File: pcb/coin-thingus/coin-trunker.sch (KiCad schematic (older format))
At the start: 30 parts, among them J1 6P6C, J2 6P6C, J3 Conn_02x20_Odd_Even, J4 Barrel_Jack_Switch_MountingPin, J5 Screw_Terminal_01x02, K1 AGQ200A4, K2 AGQ200A4, Q1 BSS123L, U1 ULN2003LV, U4 TCA9534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

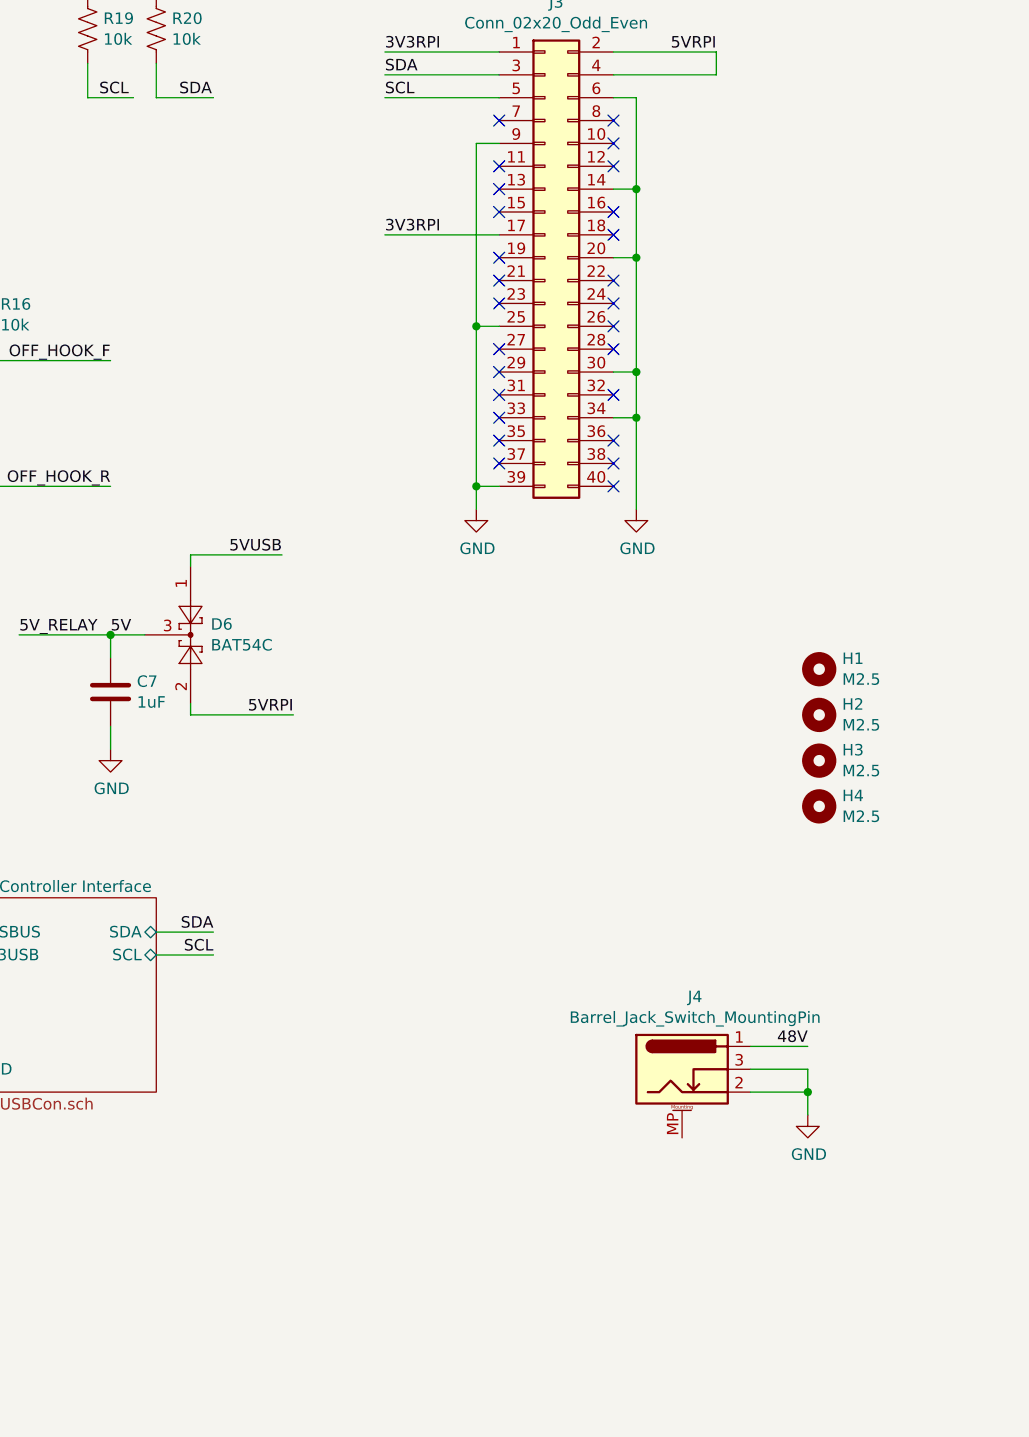
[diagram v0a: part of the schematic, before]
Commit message: Add CERN-OHL-W v2 license
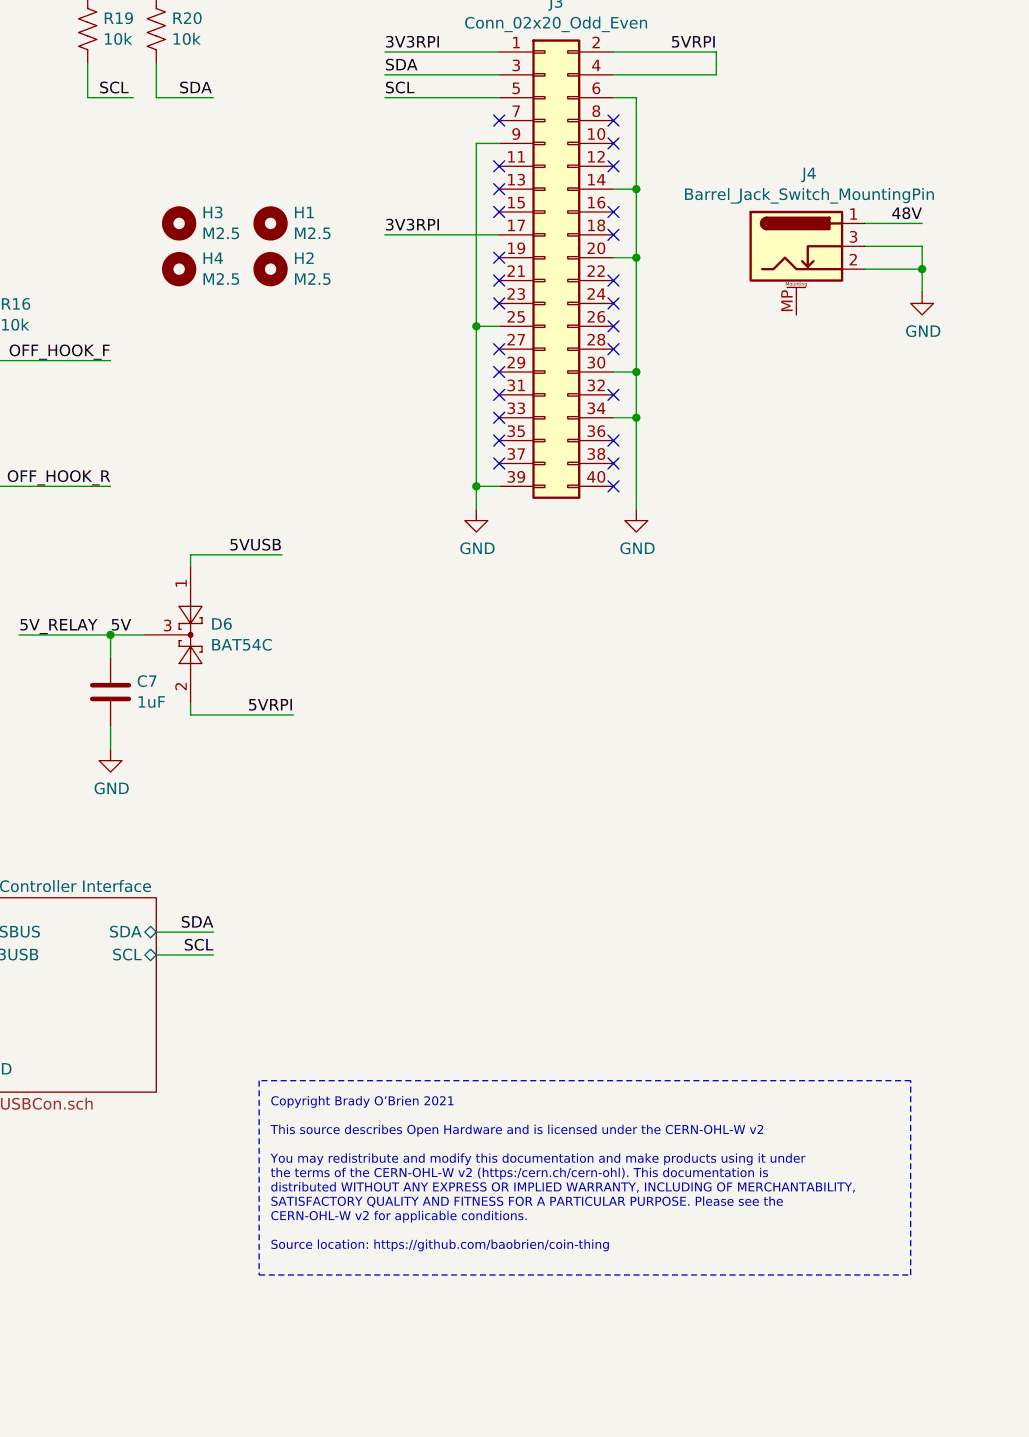
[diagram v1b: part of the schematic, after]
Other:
- note added: "Copyright Brady O’Brien 2021\n\nThis source describes Open Hardware and is licensed under the CERN-OHL-W v2\n\nYou may redistribute and modify this documentation and make products using it under\nthe terms of the CERN-OHL-W v2 (https:/cern.ch/cern-ohl). This documentation is\ndistributed WITHOUT ANY EXPRESS OR IMPLIED WARRANTY, INCLUDING OF MERCHANTABILITY,\nSATISFACTORY QUALITY AND FITNESS FOR A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"
- moved on the sheet: H1, H2, H3, H4, J4
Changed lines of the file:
@@
 L Connector:Barrel_Jack_Switch_MountingPin J4
 U 1 1 5F9413CC
-P 9850 5400
-F 0 "J4" H 9907 5717 50  0000 C CNN
-F 1 "Barrel_Jack_Switch_MountingPin" H 9907 5626 50  0000 C CNN
-F 2 "Connector_BarrelJack:BarrelJack_CUI_PJ-102AH_Horizontal" H 9900 5360 50  0001 C CNN
-F 3 "~" H 9900 5360 50  0001 C CNN
-F 4 "PJ-102AH" H 9850 5400 50  0001 C CNN "Part"
-	1    9850 5400
+P 10350 1800
+F 0 "J4" H 10407 2117 50  0000 C CNN
+F 1 "Barrel_Jack_Switch_MountingPin" H 10407 2026 50  0000 C CNN
+F 2 "Connector_BarrelJack:BarrelJack_CUI_PJ-102AH_Horizontal" H 10400 1760 50  0001 C CNN
+F 3 "~" H 10400 1760 50  0001 C CNN
+F 4 "PJ-102AH" H 10350 1800 50  0001 C CNN "Part"
+	1    10350 1800
 	1    0    0    -1
 $EndComp
@@
 L power:GND #PWR0101
 U 1 1 5F942022
-P 10400 5600
-F 0 "#PWR0101" H 10400 5350 50  0001 C CNN
-F 1 "GND" H 10405 5427 50  0000 C CNN
-F 2 "" H 10400 5600 50  0001 C CNN
-F 3 "" H 10400 5600 50  0001 C CNN
-	1    10400 5600
-	1    0    0    -1
-$EndComp
-Wire Wire Line
-	10150 5400 10400 5400
-Wire Wire Line
-	10400 5400 10400 5500
-Wire Wire Line
-	10150 5500 10400 5500
-Connection ~ 10400 5500
-Wire Wire Line
-	10400 5500 10400 5600
-Wire Wire Line
-	10400 5300 10150 5300
-Text Label 10400 5300 2    50   ~ 0
+P 10900 2000
+F 0 "#PWR0101" H 10900 1750 50  0001 C CNN
+F 1 "GND" H 10905 1827 50  0000 C CNN
+F 2 "" H 10900 2000 50  0001 C CNN
+F 3 "" H 10900 2000 50  0001 C CNN
+	1    10900 2000
+	1    0    0    -1
+$EndComp
+Wire Wire Line
+	10650 1800 10900 1800
+Wire Wire Line
+	10900 1800 10900 1900
+Wire Wire Line
+	10650 1900 10900 1900
+Connection ~ 10900 1900
+Wire Wire Line
+	10900 1900 10900 2000
+Wire Wire Line
+	10900 1700 10650 1700
+Text Label 10900 1700 2    50   ~ 0
 48V
 $Sheet
@@
 L Mechanical:MountingHole H1
 U 1 1 5FDD0277
-P 10450 3650
-F 0 "H1" H 10550 3696 50  0000 L CNN
-F 1 "M2.5" H 10550 3605 50  0000 L CNN
-F 2 "MountingHole:MountingHole_2.7mm_M2.5_Pad" H 10450 3650 50  0001 C CNN
-F 3 "~" H 10450 3650 50  0001 C CNN
-	1    10450 3650
+P 8050 1700
+F 0 "H1" H 8150 1746 50  0000 L CNN
+F 1 "M2.5" H 8150 1655 50  0000 L CNN
+F 2 "MountingHole:MountingHole_2.7mm_M2.5_Pad" H 8050 1700 50  0001 C CNN
+F 3 "~" H 8050 1700 50  0001 C CNN
+	1    8050 1700
 	1    0    0    -1
 $EndComp
@@
 L Mechanical:MountingHole H2
 U 1 1 5FDDD6B4
-P 10450 3850
-F 0 "H2" H 10550 3896 50  0000 L CNN
-F 1 "M2.5" H 10550 3805 50  0000 L CNN
-F 2 "MountingHole:MountingHole_2.7mm_M2.5_Pad" H 10450 3850 50  0001 C CNN
-F 3 "~" H 10450 3850 50  0001 C CNN
-	1    10450 3850
+P 8050 1900
+F 0 "H2" H 8150 1946 50  0000 L CNN
+F 1 "M2.5" H 8150 1855 50  0000 L CNN
+F 2 "MountingHole:MountingHole_2.7mm_M2.5_Pad" H 8050 1900 50  0001 C CNN
+F 3 "~" H 8050 1900 50  0001 C CNN
+	1    8050 1900
 	1    0    0    -1
 $EndComp
@@
 L Mechanical:MountingHole H3
 U 1 1 5FDDDD20
-P 10450 4050
-F 0 "H3" H 10550 4096 50  0000 L CNN
-F 1 "M2.5" H 10550 4005 50  0000 L CNN
-F 2 "MountingHole:MountingHole_2.7mm_M2.5_Pad" H 10450 4050 50  0001 C CNN
-F 3 "~" H 10450 4050 50  0001 C CNN
-	1    10450 4050
+P 7650 1700
+F 0 "H3" H 7750 1746 50  0000 L CNN
+F 1 "M2.5" H 7750 1655 50  0000 L CNN
+F 2 "MountingHole:MountingHole_2.7mm_M2.5_Pad" H 7650 1700 50  0001 C CNN
+F 3 "~" H 7650 1700 50  0001 C CNN
+	1    7650 1700
 	1    0    0    -1
 $EndComp
@@
 L Mechanical:MountingHole H4
 U 1 1 5FDDDF7B
-P 10450 4250
-F 0 "H4" H 10550 4296 50  0000 L CNN
-F 1 "M2.5" H 10550 4205 50  0000 L CNN
-F 2 "MountingHole:MountingHole_2.7mm_M2.5_Pad" H 10450 4250 50  0001 C CNN
-F 3 "~" H 10450 4250 50  0001 C CNN
-	1    10450 4250
+P 7650 1900
+F 0 "H4" H 7750 1946 50  0000 L CNN
+F 1 "M2.5" H 7750 1855 50  0000 L CNN
+F 2 "MountingHole:MountingHole_2.7mm_M2.5_Pad" H 7650 1900 50  0001 C CNN
+F 3 "~" H 7650 1900 50  0001 C CNN
+	1    7650 1900
 	1    0    0    -1
 $EndComp
@@
 Wire Wire Line
 	3000 3650 3650 3650
+Text Notes 8050 6200 0    39   ~ 0
+Copyright Brady O’Brien 2021\n\nThis source describes Open Hardware and is licensed under the CERN-OHL-W v2\n\nYou may redistribute and modify this documentation and make products using it under\nthe terms of the CERN-OHL-W v2 (https:/cern.ch/cern-ohl). This documentation is\ndistributed WITHOUT ANY EXPRESS OR IMPLIED WARRANTY, INCLUDING OF MERCHANTABILITY,\nSATISFACTORY QUALITY AND FITNESS FOR A PARTICULAR PURPOSE. Please see the\nCERN-OHL-W v2 for applicable conditions.\n\nSource location: https://github.com/baobrien/coin-thing
+Wire Notes Line
+	8000 5450 8000 6300
+Wire Notes Line
+	8000 6300 10850 6300
+Wire Notes Line
+	10850 6300 10850 5450
+Wire Notes Line
+	10850 5450 8000 5450
 $EndSCHEMATC

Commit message: Some work towards v0.2
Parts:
- removed U5: ILD74, Package_DIP:DIP-8_W7.62mm, symbol Isolator:ILD74
- added U5, U8: LTV-217, Package_SO:SOP-4_4.4x2.6mm_P1.27mm, symbol coin_trunker_parts:LTV-217
- J5: footprint TerminalBlock_Phoenix:TerminalBlock_Phoenix_MPT-0,5-2-2.54_1x02_P2.54mm_Horizontal -> (none)
- K1, K2: value AGQ200A4 -> HFD4/5-S
- R10: footprint Resistor_SMD:R_0612_1632Metric -> Resistor_SMD:R_1206_3216Metric
- U1: footprint Package_SO:SOIC-16W_5.3x10.2mm_P1.27mm -> Package_SO:SOIC-16_3.9x9.9mm_P1.27mm
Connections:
- wire segments 181 -> 177
- no-connect marks 38 -> 37
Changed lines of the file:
@@
 Wire Wire Line
 	2350 1700 2250 1700
-Text Label 3300 1600 2    50   ~ 0
+Text Label 3250 1800 2    50   ~ 0
 T_COIN
 Wire Wire Line
@@
 F 0 "U1" H 2350 3817 50  0000 C CNN
 F 1 "ULN2003LV" H 2350 3726 50  0000 C CNN
-F 2 "Package_SO:SOIC-16W_5.3x10.2mm_P1.27mm" H 2400 2600 50  0001 L CNN
+F 2 "Package_SO:SOIC-16_3.9x9.9mm_P1.27mm" H 2400 2600 50  0001 L CNN
 F 3 "http://www.ti.com/lit/ds/symlink/uln2003a.pdf" H 2450 2950 50  0001 C CNN
 	1    2350 3150
@@
 	2250 1550 2250 1700
 $Comp
-L Isolator:ILD74 U5
-U 1 1 5FBB4DF0
-P 5950 2400
-F 0 "U5" H 5950 2725 50  0000 C CNN
-F 1 "ILD74" H 5950 2634 50  0000 C CNN
-F 2 "Package_DIP:DIP-8_W7.62mm" H 5750 2200 50  0001 L CIN
-F 3 "https://www.vishay.com/docs/83640/ild74.pdf" H 5950 2400 50  0001 L CNN
-	1    5950 2400
-	1    0    0    -1
-$EndComp
-$Comp
-L Isolator:ILD74 U5
-U 2 1 5FBB5638
-P 5950 2950
-F 0 "U5" H 5950 3275 50  0000 C CNN
-F 1 "ILD74" H 5950 3184 50  0000 C CNN
-F 2 "Package_DIP:DIP-8_W7.62mm" H 5750 2750 50  0001 L CIN
-F 3 "https://www.vishay.com/docs/83640/ild74.pdf" H 5950 2950 50  0001 L CNN
-	2    5950 2950
-	1    0    0    -1
-$EndComp
-$Comp
 L Device:R_US R10
 U 1 1 5FBB6E50
@@
 F 0 "R10" V 3545 2250 50  0000 C CNN
 F 1 "120 2W" V 3636 2250 50  0000 C CNN
-F 2 "Resistor_SMD:R_0612_1632Metric" V 3790 2240 50  0001 C CNN
+F 2 "Resistor_SMD:R_1206_3216Metric" V 3790 2240 50  0001 C CNN
 F 3 "~" H 3750 2250 50  0001 C CNN
 	1    3750 2250
@@
 OFF_HOOK_R
 Wire Wire Line
-	3450 1400 3450 1200
-Wire Wire Line
-	3450 1200 4250 1200
-Wire Wire Line
-	2950 1400 3450 1400
-Wire Wire Line
-	4250 1600 3400 1600
-Wire Wire Line
-	3400 1600 3400 1800
-Wire Wire Line
-	2950 1800 3400 1800
-Wire Wire Line
 	3350 6200 3550 6200
 Wire Wire Line
@@
 F 0 "J5" H 1818 6525 50  0000 C CNN
 F 1 "Screw_Terminal_01x02" H 1818 6616 50  0000 C CNN
-F 2 "TerminalBlock_Phoenix:TerminalBlock_Phoenix_MPT-0,5-2-2.54_1x02_P2.54mm_Horizontal" H 1900 6850 50  0001 C CNN
+F 2 "" H 1900 6850 50  0001 C CNN
 F 3 "~" H 1900 6850 50  0001 C CNN
 F 4 "1725656" H 1900 6850 50  0001 C CNN "Part"
@@
 NoConn ~ 1350 1350
 NoConn ~ 1350 1650
-Wire Wire Line
-	3300 1600 2950 1600
-NoConn ~ 2950 1200
 NoConn ~ 5650 1200
 NoConn ~ 5650 1500
@@
 $Comp
 L Relay:IM00 K?
-U 1 1 5FE20380
-P 2650 1300
-AR Path="/5FA767FA/5FE20380" Ref="K?"  Part="1"
-AR Path="/5FE20380" Ref="K1"  Part="1"
-F 0 "K1" V 1883 1300 50  0000 C CNN
-F 1 "AGQ200A4" V 1974 1300 50  0000 C CNN
-F 2 "Relay_SMD:Relay_DPDT_Omron_G6K-2F-Y" H 2450 1300 50  0001 C CNN
-F 3 "" H 2450 1300 50  0001 C CNN
-	1    2650 1300
-	0    1    1    0
-$EndComp
-$Comp
-L Relay:IM00 K?
 U 1 1 5FE2C154
 P 4550 1300
@@
 AR Path="/5FE2C154" Ref="K2"  Part="1"
 F 0 "K2" V 3783 1300 50  0000 C CNN
-F 1 "AGQ200A4" V 3874 1300 50  0000 C CNN
+F 1 "HFD4/5-S" V 3874 1300 50  0000 C CNN
 F 2 "Relay_SMD:Relay_DPDT_Omron_G6K-2F-Y" H 4350 1300 50  0001 C CNN
 F 3 "" H 4350 1300 50  0001 C CNN
@@
 Wire Notes Line
 	10850 5450 8000 5450
+$Comp
+L Relay:IM00 K?
+U 1 1 5FE20380
+P 2650 1300
+AR Path="/5FA767FA/5FE20380" Ref="K?"  Part="1"
+AR Path="/5FE20380" Ref="K1"  Part="1"
+F 0 "K1" V 1883 1300 50  0000 C CNN
+F 1 "HFD4/5-S" V 1974 1300 50  0000 C CNN
+F 2 "Relay_SMD:Relay_DPDT_Omron_G6K-2F-Y" H 2450 1300 50  0001 C CNN
+F 3 "" H 2450 1300 50  0001 C CNN
+	1    2650 1300
+	0    1    1    0
+$EndComp
+Wire Wire Line
+	2950 1200 4250 1200
+Wire Wire Line
+	2950 1600 4250 1600
+Wire Wire Line
+	3250 1800 2950 1800
+$Comp
+L coin_trunker_parts:LTV-217 U5
+U 1 1 6033624A
+P 5950 2400
+F 0 "U5" H 5950 2725 50  0000 C CNN
+F 1 "LTV-217" H 5950 2634 50  0000 C CNN
+F 2 "Package_SO:SOP-4_4.4x2.6mm_P1.27mm" H 5750 2200 50  0001 L CIN
+F 3 "http://optoelectronics.liteon.com/upload/download/DS70-2009-0014/LTV-2X7%20sereis%20Mar17.PDF" H 5950 2400 50  0001 L CNN
+	1    5950 2400
+	1    0    0    -1
+$EndComp
+$Comp
+L coin_trunker_parts:LTV-217 U8
+U 1 1 6033877C
+P 5950 2950
+F 0 "U8" H 5950 3275 50  0000 C CNN
+F 1 "LTV-217" H 5950 3184 50  0000 C CNN
+F 2 "Package_SO:SOP-4_4.4x2.6mm_P1.27mm" H 5750 2750 50  0001 L CIN
+F 3 "http://optoelectronics.liteon.com/upload/download/DS70-2009-0014/LTV-2X7%20sereis%20Mar17.PDF" H 5950 2950 50  0001 L CNN
+	1    5950 2950
+	1    0    0    -1
+$EndComp
 $EndSCHEMATC

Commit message: HV test board; A bunch of work towards v0.2
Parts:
- removed J5: Screw_Terminal_01x02, symbol Connector:Screw_Terminal_01x02
- added D10, D11, D12, D7, D9: LED, LED_SMD:LED_0603_1608Metric, symbol Device:LED
- added J5: Screw_Terminal_01x01, coin-trunker:screw_block_m3_5x7, symbol Connector:Screw_Terminal_01x01
- added R21, R22, R23, R24, R25: 470, Resistor_SMD:R_0603_1608Metric, symbol Device:R_US
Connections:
- wire segments 177 -> 194
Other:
- note added: "Blinkinlights"
- moved on the sheet: J3, J4

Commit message: Bunch'o work towards v0.2
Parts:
- added C13: 1uF, Capacitor_SMD:C_0603_1608Metric, symbol Device:C
- added C14, C15: 270pF, Capacitor_SMD:C_0603_1608Metric, symbol Device:C
- added D15: 1N4148WS, Diode_SMD:D_SOD-323_HandSoldering, symbol Device:D
- added JP1, JP2: SolderJumper_2_Open, Jumper:SolderJumper-2_P1.3mm_Open_TrianglePad1.0x1.5mm, symbol Jumper:SolderJumper_2_Open
- added Q4: BSS84, Package_TO_SOT_SMD:SOT-23, symbol Device:Q_PMOS_GSD
- added R27: 10k, Resistor_SMD:R_0603_1608Metric, symbol Device:R_US
- added R28: 500k, Resistor_SMD:R_0603_1608Metric, symbol Device:R_US
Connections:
- net labels added: CT_LV_L
- wire segments 194 -> 237
- no-connect marks 37 -> 35
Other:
- note added: "Coin test time limiter"
- note added: "Optional jumpers to \nearth board through \nphone line"
- note added: "Prevents coin-test relay for being \nheld for more than 250ms"
- note added: "R7 in coin test circuit dissipates\nup to 5W in coin-test mode"
- moved on the sheet: C5, J4, J5, R19, R20

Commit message: Coin thing v0.2 PCB
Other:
- note added: "Blinkenlights"
- note removed: "Blinkinlights"
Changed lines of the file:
@@
 	9450 4350 10300 4350
 Text Notes 9150 4550 0    50   ~ 0
-Blinkinlights
+Blinkenlights
 Text Label 10300 3850 2    50   ~ 0
 COIN_TEST_RELAY

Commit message: Start work on alternate micro
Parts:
- R1, R11, R12, R13, R14, R15, R16, R19, R20, R21, R22, R23, R24, R25, R27, R28: footprint Resistor_SMD:R_0603_1608Metric -> Resistor_SMD:R_0402_1005Metric
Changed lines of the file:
@@
 F 0 "R15" H 6382 2054 50  0000 R CNN
 F 1 "10k" H 6382 2145 50  0000 R CNN
-F 2 "Resistor_SMD:R_0603_1608Metric" V 6490 2090 50  0001 C CNN
+F 2 "Resistor_SMD:R_0402_1005Metric" V 6490 2090 50  0001 C CNN
 F 3 "~" H 6450 2100 50  0001 C CNN
 	1    6450 2100
@@
 F 0 "R16" H 6732 2054 50  0000 R CNN
 F 1 "10k" H 6732 2145 50  0000 R CNN
-F 2 "Resistor_SMD:R_0603_1608Metric" V 6840 2090 50  0001 C CNN
+F 2 "Resistor_SMD:R_0402_1005Metric" V 6840 2090 50  0001 C CNN
 F 3 "~" H 6800 2100 50  0001 C CNN
 	1    6800 2100
@@
 F 0 "R13" V 5350 1350 50  0000 C CNN
 F 1 "120" V 5364 1500 50  0000 C CNN
-F 2 "Resistor_SMD:R_0603_1608Metric" V 5290 1490 50  0001 C CNN
+F 2 "Resistor_SMD:R_0402_1005Metric" V 5290 1490 50  0001 C CNN
 F 3 "~" H 5250 1500 50  0001 C CNN
 	1    5250 1500
@@
 F 0 "R11" H 4782 3354 50  0000 R CNN
 F 1 "10k" H 4782 3445 50  0000 R CNN
-F 2 "Resistor_SMD:R_0603_1608Metric" V 4890 3390 50  0001 C CNN
+F 2 "Resistor_SMD:R_0402_1005Metric" V 4890 3390 50  0001 C CNN
 F 3 "~" H 4850 3400 50  0001 C CNN
 	1    4850 3400
@@
 F 0 "R12" H 5082 3354 50  0000 R CNN
 F 1 "10k" H 5082 3445 50  0000 R CNN
-F 2 "Resistor_SMD:R_0603_1608Metric" V 5190 3390 50  0001 C CNN
+F 2 "Resistor_SMD:R_0402_1005Metric" V 5190 3390 50  0001 C CNN
 F 3 "~" H 5150 3400 50  0001 C CNN
 	1    5150 3400
@@
 F 0 "R14" H 5382 3354 50  0000 R CNN
 F 1 "10k" H 5382 3445 50  0000 R CNN
-F 2 "Resistor_SMD:R_0603_1608Metric" V 5490 3390 50  0001 C CNN
+F 2 "Resistor_SMD:R_0402_1005Metric" V 5490 3390 50  0001 C CNN
 F 3 "~" H 5450 3400 50  0001 C CNN
 	1    5450 3400
@@
 F 0 "R1" H 1718 4296 50  0000 L CNN
 F 1 "10k" H 1718 4205 50  0000 L CNN
-F 2 "Resistor_SMD:R_0603_1608Metric" V 1690 4240 50  0001 C CNN
+F 2 "Resistor_SMD:R_0402_1005Metric" V 1690 4240 50  0001 C CNN
 F 3 "~" H 1650 4250 50  0001 C CNN
 	1    1650 4250
@@
 F 0 "R20" H 6982 854 50  0000 R CNN
 F 1 "10k" H 6982 945 50  0000 R CNN
-F 2 "Resistor_SMD:R_0603_1608Metric" V 7090 890 50  0001 C CNN
+F 2 "Resistor_SMD:R_0402_1005Metric" V 7090 890 50  0001 C CNN
 F 3 "~" H 7050 900 50  0001 C CNN
 	1    7050 900
@@
 F 0 "R19" H 6682 854 50  0000 R CNN
 F 1 "10k" H 6682 945 50  0000 R CNN
-F 2 "Resistor_SMD:R_0603_1608Metric" V 6790 890 50  0001 C CNN
+F 2 "Resistor_SMD:R_0402_1005Metric" V 6790 890 50  0001 C CNN
 F 3 "~" H 6750 900 50  0001 C CNN
 	1    6750 900
@@
 F 0 "R21" V 8800 3300 50  0000 R CNN
 F 1 "470" V 8800 3500 50  0000 R CNN
-F 2 "Resistor_SMD:R_0603_1608Metric" V 8940 3340 50  0001 C CNN
+F 2 "Resistor_SMD:R_0402_1005Metric" V 8940 3340 50  0001 C CNN
 F 3 "~" H 8900 3350 50  0001 C CNN
 	1    8900 3350
@@
 F 0 "R22" V 8800 3550 50  0000 R CNN
 F 1 "470" V 8800 3750 50  0000 R CNN
-F 2 "Resistor_SMD:R_0603_1608Metric" V 8940 3590 50  0001 C CNN
+F 2 "Resistor_SMD:R_0402_1005Metric" V 8940 3590 50  0001 C CNN
 F 3 "~" H 8900 3600 50  0001 C CNN
 	1    8900 3600
@@
 F 0 "R23" V 8800 3800 50  0000 R CNN
 F 1 "470" V 8800 4000 50  0000 R CNN
-F 2 "Resistor_SMD:R_0603_1608Metric" V 8940 3840 50  0001 C CNN
+F 2 "Resistor_SMD:R_0402_1005Metric" V 8940 3840 50  0001 C CNN
 F 3 "~" H 8900 3850 50  0001 C CNN
 	1    8900 3850
@@
 F 0 "R24" V 8800 4050 50  0000 R CNN
 F 1 "470" V 8800 4250 50  0000 R CNN
-F 2 "Resistor_SMD:R_0603_1608Metric" V 8940 4090 50  0001 C CNN
+F 2 "Resistor_SMD:R_0402_1005Metric" V 8940 4090 50  0001 C CNN
 F 3 "~" H 8900 4100 50  0001 C CNN
 	1    8900 4100
@@
 F 0 "R25" V 8800 4300 50  0000 R CNN
 F 1 "470" V 8800 4500 50  0000 R CNN
-F 2 "Resistor_SMD:R_0603_1608Metric" V 8940 4340 50  0001 C CNN
+F 2 "Resistor_SMD:R_0402_1005Metric" V 8940 4340 50  0001 C CNN
 F 3 "~" H 8900 4350 50  0001 C CNN
 	1    8900 4350
@@
 F 0 "R28" H 3150 5050 50  0000 L CNN
 F 1 "500k" H 3100 5150 50  0000 L CNN
-F 2 "Resistor_SMD:R_0603_1608Metric" V 3340 4940 50  0001 C CNN
+F 2 "Resistor_SMD:R_0402_1005Metric" V 3340 4940 50  0001 C CNN
 F 3 "~" H 3300 4950 50  0001 C CNN
 	1    3300 4950
@@
 F 0 "R27" H 2818 5446 50  0000 L CNN
 F 1 "10k" H 2818 5355 50  0000 L CNN
-F 2 "Resistor_SMD:R_0603_1608Metric" V 2790 5390 50  0001 C CNN
+F 2 "Resistor_SMD:R_0402_1005Metric" V 2790 5390 50  0001 C CNN
 F 3 "~" H 2750 5400 50  0001 C CNN
 	1    2750 5400
